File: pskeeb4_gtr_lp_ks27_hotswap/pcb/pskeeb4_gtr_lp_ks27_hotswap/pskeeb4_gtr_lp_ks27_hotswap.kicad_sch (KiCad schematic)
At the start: 45 parts, among them K1 KEYSW, K10 KEYSW, K11 KEYSW, K12 KEYSW, K13 KEYSW, K14 KEYSW, K15 KEYSW, K16 KEYSW, K17 KEYSW, K18 KEYSW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

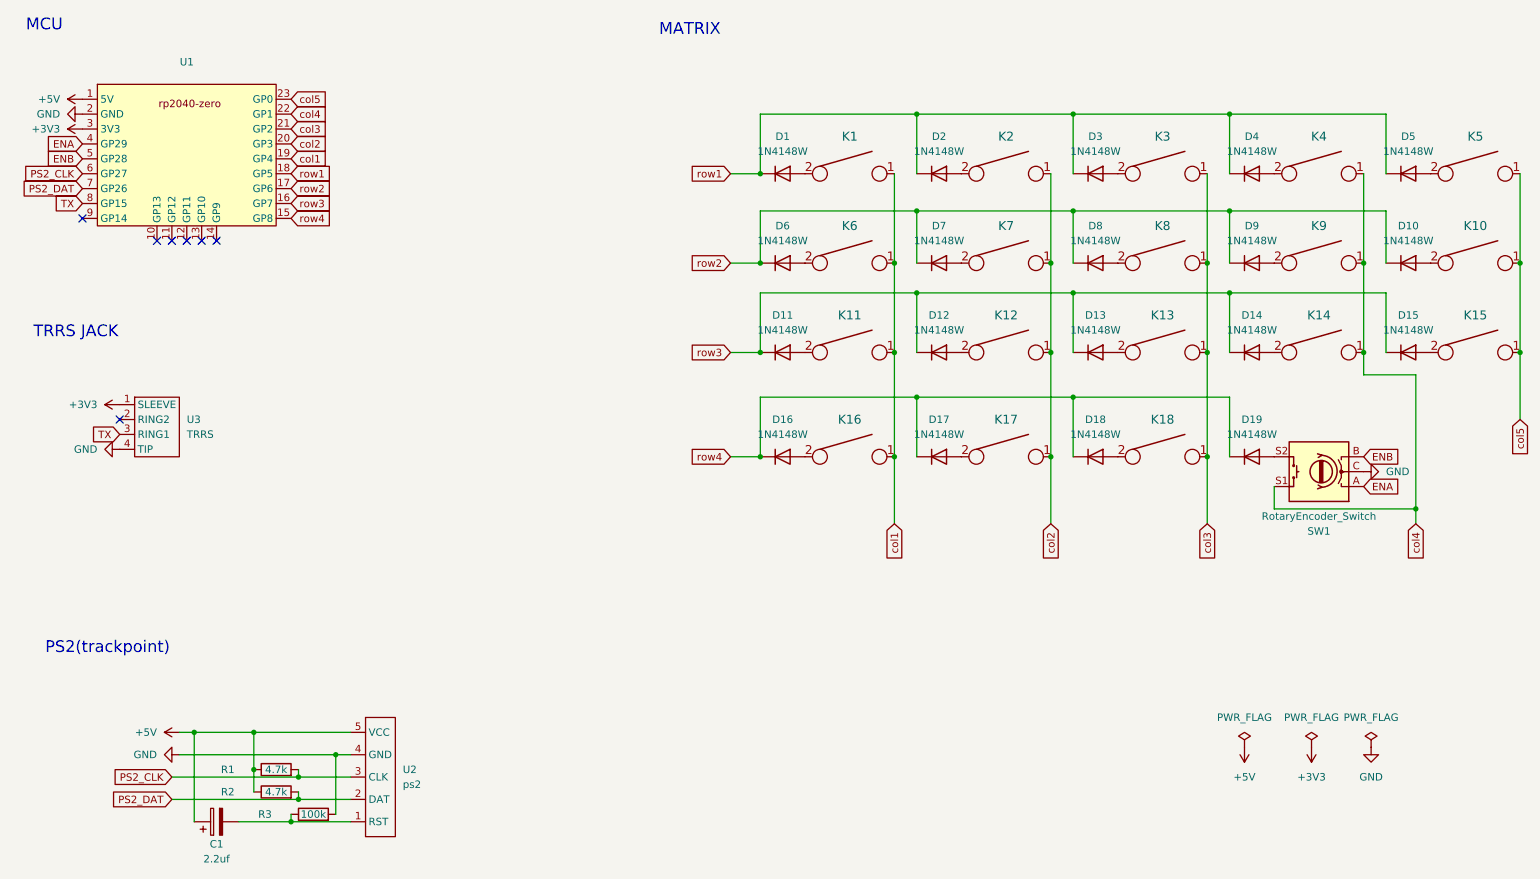
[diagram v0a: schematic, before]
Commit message: feat: added hugebug trackball
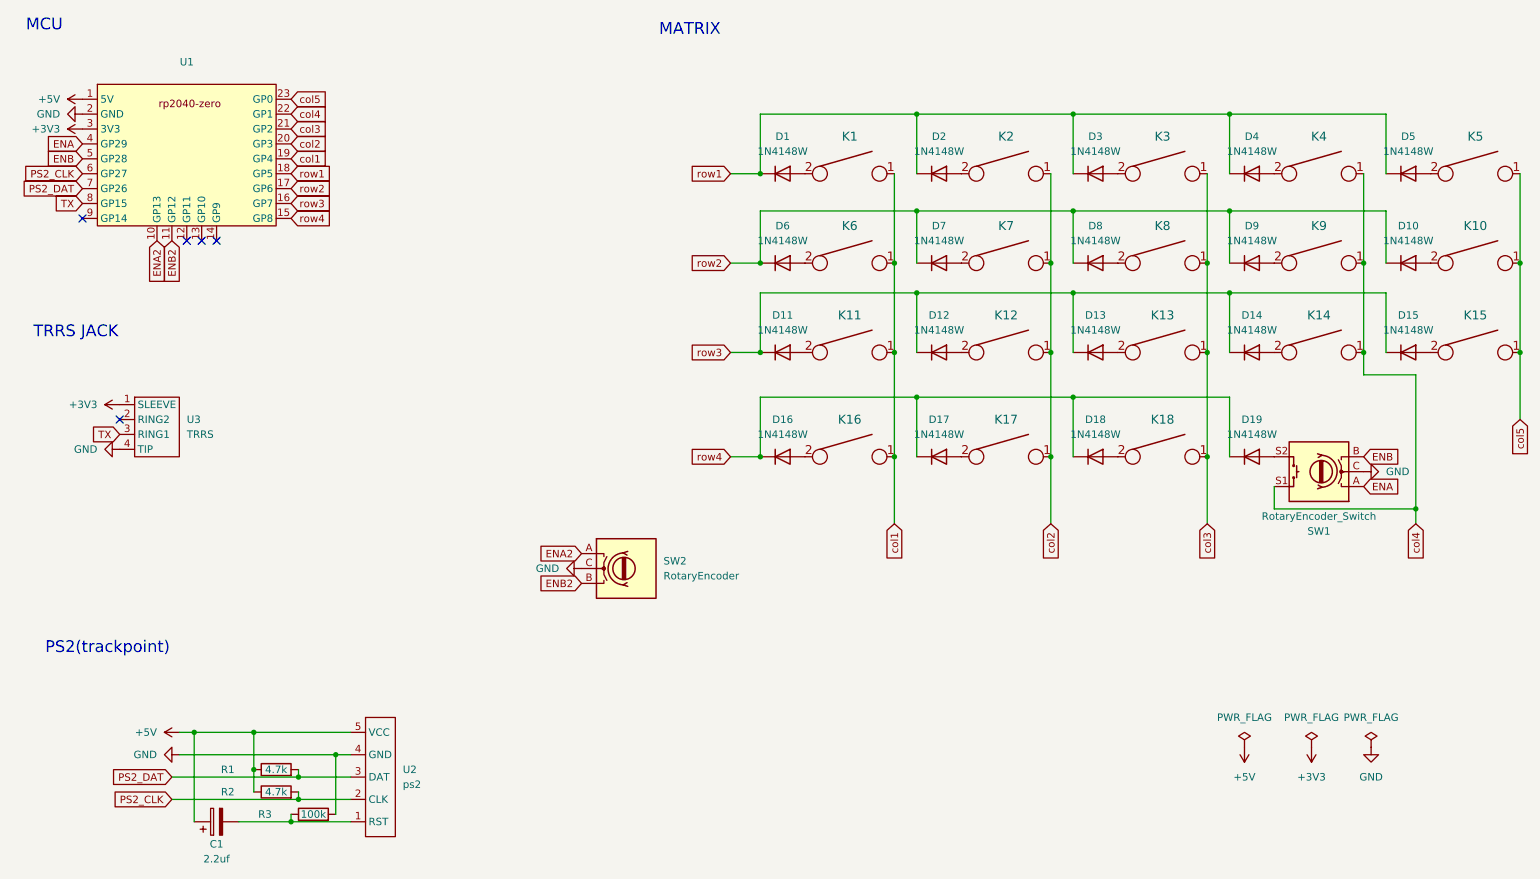
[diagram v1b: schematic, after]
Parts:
- added SW2: RotaryEncoder, kwkb-footprint:nobole-rotary-encoder, symbol Device:RotaryEncoder
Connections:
- net GND: now also SW2.C
- net PS2_CLK: now also R2.2, U2.2 (CLK); no longer R1.2, U2.3 (CLK)
- net PS2_DAT: now also R1.2, U2.3 (DAT); no longer R2.2, U2.2 (DAT)
- net ENA2: now reaches U1.10 (GP13)
- net ENA2: now also SW2.A
- net ENB2: now reaches U1.11 (GP12)
- net ENB2: now also SW2.B
- no-connect marks 7 -> 5
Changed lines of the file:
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@@
 	)
 	(no_connect
-		(at 44.45 59.69)
-	)
-	(no_connect
 		(at 31.75 55.88)
 	)
@@
 	)
 	(no_connect
-		(at 46.99 59.69)
-	)
-	(no_connect
 		(at 52.07 59.69)
 	)
@@
 		)
 	)
+	(global_label "ENB2"
+		(shape input)
+		(at 46.99 59.69 270)
+		(fields_autoplaced yes)
+		(effects
+			(font
+				(size 1.27 1.27)
+			)
+			(justify right)
+		)
+		(property "Intersheetrefs" "${INTERSHEET_REFS}"
+			(at 46.99 67.6342 90)
+			(effects
+				(font
+					(size 1.27 1.27)
+				)
+				(justify right)
+				(hide yes)
+			)
+		)
+	)
 	(global_label "col1"
 		(shape input)
@@
 	(global_label "PS2_DAT"
 		(shape input)
-		(at 46.99 154.94 180)
+		(at 46.99 151.13 180)
 		(fields_autoplaced yes)
 		(effects
@@
 		)
 		(property "Intersheetrefs" "${INTERSHEET_REFS}"
-			(at 36.022 154.94 0)
+			(at 36.022 151.13 0)
 			(effects
 				(font
@@
 		)
 	)
+	(global_label "ENA2"
+		(shape input)
+		(at 44.45 59.69 270)
+		(fields_autoplaced yes)
+		(effects
+			(font
+				(size 1.27 1.27)
+			)
+			(justify right)
+		)
+		(property "Intersheetrefs" "${INTERSHEET_REFS}"
+			(at 44.45 67.4528 90)
+			(effects
+				(font
+					(size 1.27 1.27)
+				)
+				(justify right)
+				(hide yes)
+			)
+		)
+	)
 	(global_label "ENB"
 		(shape input)
@@
 		)
 	)
+	(global_label "ENA2"
+		(shape input)
+		(at 116.84 113.03 180)
+		(fields_autoplaced yes)
+		(effects
+			(font
+				(size 1.27 1.27)
+			)
+			(justify right)
+		)
+		(property "Intersheetrefs" "${INTERSHEET_REFS}"
+			(at 109.0772 113.03 0)
+			(effects
+				(font
+					(size 1.27 1.27)
+				)
+				(justify right)
+				(hide yes)
+			)
+		)
+	)
 	(global_label "PS2_CLK"
 		(shape input)
-		(at 46.99 151.13 180)
+		(at 46.99 154.94 180)
 		(fields_autoplaced yes)
 		(effects
@@
 		)
 		(property "Intersheetrefs" "${INTERSHEET_REFS}"
-			(at 35.7801 151.13 0)
+			(at 35.7801 154.94 0)
+			(effects
+				(font
+					(size 1.27 1.27)
+				)
+				(justify right)
+				(hide yes)
+			)
+		)
+	)
+	(global_label "ENB2"
+		(shape input)
+		(at 116.84 118.11 180)
+		(fields_autoplaced yes)
+		(effects
+			(font
+				(size 1.27 1.27)
+			)
+			(justify right)
+		)
+		(property "Intersheetrefs" "${INTERSHEET_REFS}"
+			(at 108.8958 118.11 0)
 			(effects
 				(font
@@
 	)
 	(symbol
+		(lib_id "Device:RotaryEncoder")
+		(at 124.46 115.57 0)
+		(unit 1)
+		(exclude_from_sim no)
+		(in_bom yes)
+		(on_board yes)
+		(dnp no)
+		(fields_autoplaced yes)
+		(property "Reference" "SW2"
+			(at 130.81 114.2999 0)
+			(effects
+				(font
+					(size 1.27 1.27)
+				)
+				(justify left)
+			)
+		)
+		(property "Value" "RotaryEncoder"
+			(at 130.81 116.8399 0)
+			(effects
+				(font
+					(size 1.27 1.27)
+				)
+				(justify left)
+			)
+		)
+		(property "Footprint" "kwkb-footprint:nobole-rotary-encoder"
+			(at 120.65 111.506 0)
+			(effects
+				(font
+					(size 1.27 1.27)
+				)
+				(hide yes)
+			)
+		)
+		(property "Datasheet" "~"
+			(at 124.46 108.966 0)
+			(effects
+				(font
+					(size 1.27 1.27)
+				)
+				(hide yes)
+			)
+		)
+		(property "Description" "Rotary encoder, dual channel, incremental quadrate outputs"
+			(at 124.46 115.57 0)
+			(effects
+				(font
+					(size 1.27 1.27)
+				)
+				(hide yes)
+			)
+		)
+		(pin "A"
+		)
+		(pin "C"
+		)
+		(pin "B"
+		)
+		(instances
+			(project ""
+				(path "/45739220-25ae-406b-a2cb-8dd202885c8a"
+					(reference "SW2")
+					(unit 1)
+				)
+			)
+		)
+	)
+	(symbol
 		(lib_name "GND_1")
 		(lib_id "power:GND")
@@
 					(unit 1)
 				)
+			)
+		)
+	)
+	(symbol
+		(lib_name "GND_1")
+		(lib_id "power:GND")
+		(at 116.84 115.57 270)
+		(unit 1)
+		(exclude_from_sim no)
+		(in_bom yes)
+		(on_board yes)
+		(dnp no)
+		(fields_autoplaced yes)
+		(property "Reference" "#PWR011"
+			(at 110.49 115.57 0)
+			(effects
+				(font
+					(size 1.27 1.27)
+				)
+				(hide yes)
+			)
+		)
+		(property "Value" "GND"
+			(at 113.03 115.5699 90)
+			(effects
+				(font
+					(size 1.27 1.27)
+				)
+				(justify right)
+			)
+		)
+		(property "Footprint" ""
+			(at 116.84 115.57 0)
+			(effects
+				(font
+					(size 1.27 1.27)
+				)
+				(hide yes)
+			)
+		)
+		(property "Datasheet" ""
+			(at 116.84 115.57 0)
+			(effects
+				(font
+					(size 1.27 1.27)
+				)
+				(hide yes)
+			)
+		)
+		(property "Description" "Power symbol creates a global label with name \"GND\" , ground"
+			(at 116.84 115.57 0)
+			(effects
+				(font
+					(size 1.27 1.27)
+				)
+				(hide yes)
+			)
+		)
+		(pin "1"
+		)
+		(instances
+			(project "pskeeb4_gtr_lp_ks27_hotswap"
+				(path "/45739220-25ae-406b-a2cb-8dd202885c8a"
+					(reference "#PWR011")
+					(unit 1)
+				)

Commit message: refactor: increase footprint pads for easier soldering
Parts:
- C1: footprint Capacitor_SMD:C_1206_3216Metric_Pad1.33x1.80mm_HandSolder -> kwkb-footprint:C_1206_3216Metric_Pad1.33x1.80mm_HandSolder
- R1, R2, R3: footprint Resistor_SMD:R_1206_3216Metric_Pad1.30x1.75mm_HandSolder -> kwkb-footprint:C_1206_3216Metric_Pad1.33x1.80mm_HandSolder
- U2: footprint Connector_JST:JST_GH_BM05B-GHS-TBT_1x05-1MP_P1.25mm_Vertical -> kwkb-footprint:JST_GH_BM05B-GHS-TBT_1x05-1MP_P1.25mm_Vertical
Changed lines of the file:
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@@
 			)
 		)
-		(property "Footprint" "Connector_JST:JST_GH_BM05B-GHS-TBT_1x05-1MP_P1.25mm_Vertical"
+		(property "Footprint" "kwkb-footprint:JST_GH_BM05B-GHS-TBT_1x05-1MP_P1.25mm_Vertical"
 			(at 77.47 140.97 0)
 			(effects
@@
 			)
 		)
-		(property "Footprint" "Resistor_SMD:R_1206_3216Metric_Pad1.30x1.75mm_HandSolder"
+		(property "Footprint" "kwkb-footprint:C_1206_3216Metric_Pad1.33x1.80mm_HandSolder"
 			(at 71.12 159.258 90)
 			(effects
@@
 			)
 		)
-		(property "Footprint" "Capacitor_SMD:C_1206_3216Metric_Pad1.33x1.80mm_HandSolder"
+		(property "Footprint" "kwkb-footprint:C_1206_3216Metric_Pad1.33x1.80mm_HandSolder"
 			(at 58.42 157.7848 0)
 			(effects
@@
 			)
 		)
-		(property "Footprint" "Resistor_SMD:R_1206_3216Metric_Pad1.30x1.75mm_HandSolder"
+		(property "Footprint" "kwkb-footprint:C_1206_3216Metric_Pad1.33x1.80mm_HandSolder"
 			(at 64.77 155.448 90)
 			(effects
@@
 			)
 		)
-		(property "Footprint" "Resistor_SMD:R_1206_3216Metric_Pad1.30x1.75mm_HandSolder"
+		(property "Footprint" "kwkb-footprint:C_1206_3216Metric_Pad1.33x1.80mm_HandSolder"
 			(at 64.77 151.638 90)
 			(effects
